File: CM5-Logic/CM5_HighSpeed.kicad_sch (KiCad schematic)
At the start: 12 parts, among them J11 690-019-298-412, J12 USB3_A, U3 AP22653W6, U4 RT9742SNGV

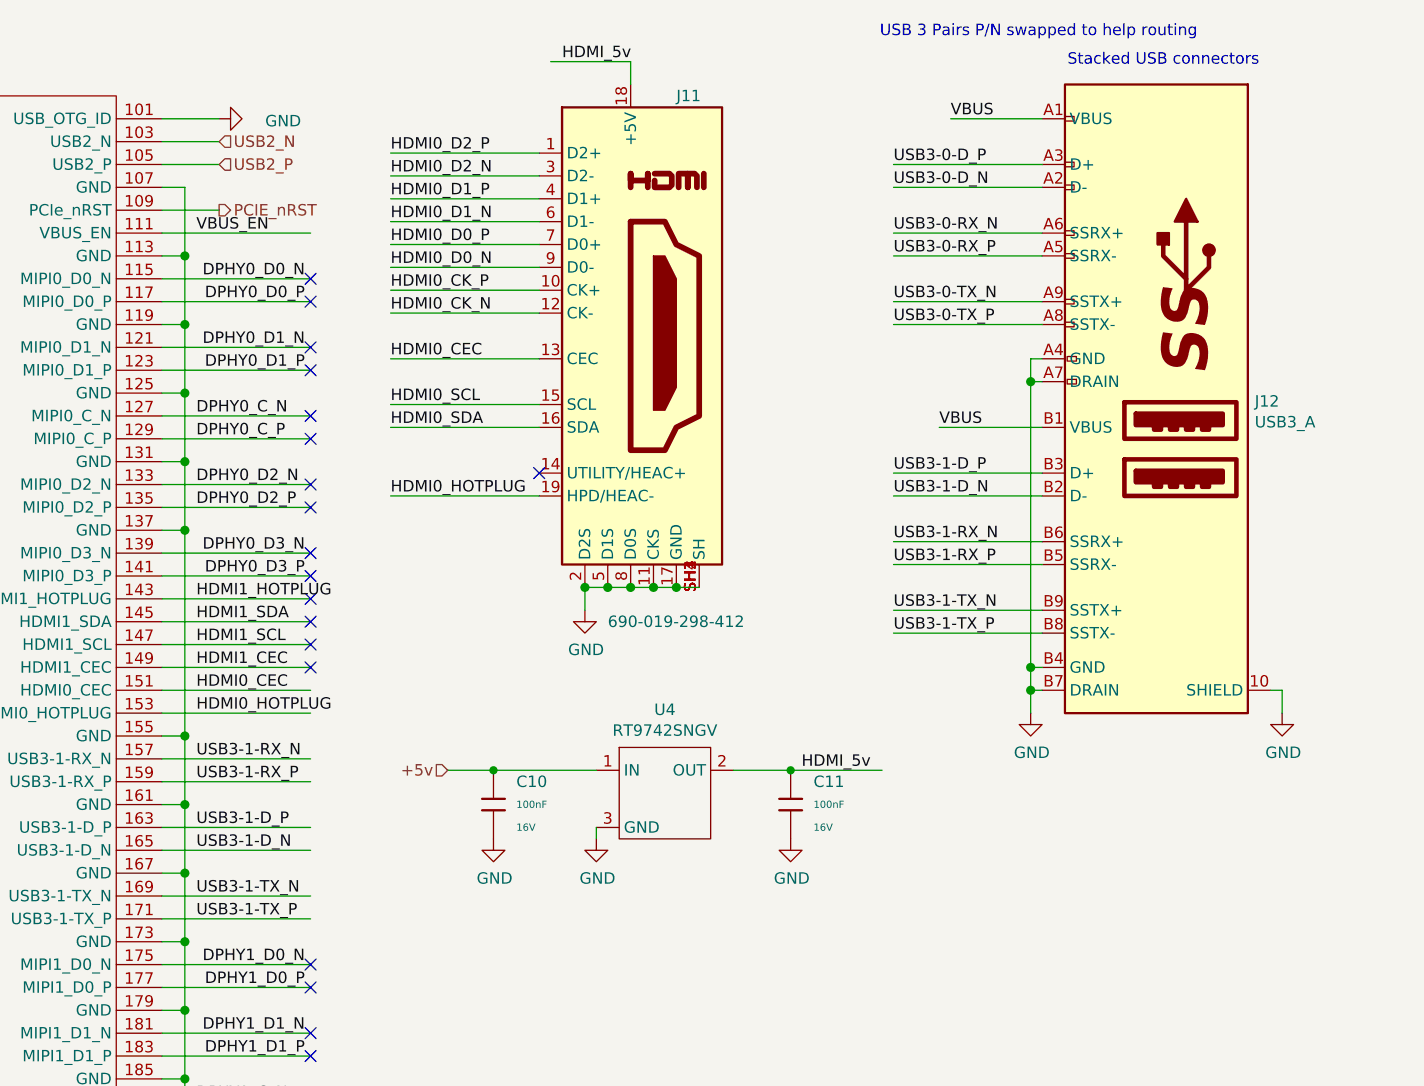
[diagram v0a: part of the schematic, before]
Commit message: adds respeaker and reworks the amplifier
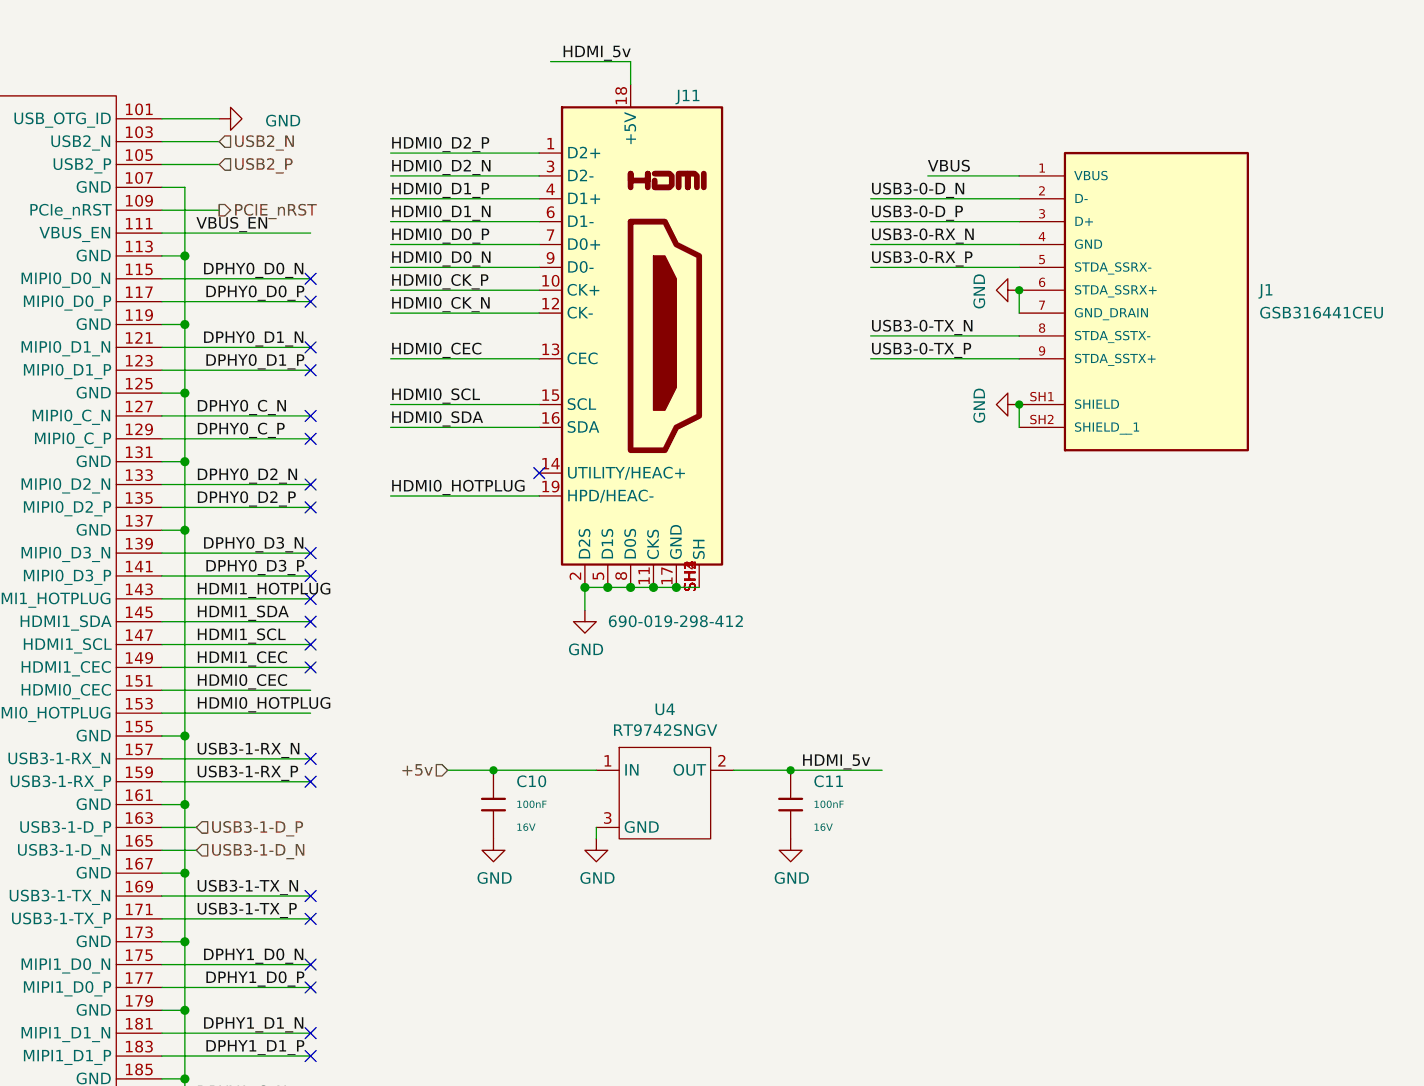
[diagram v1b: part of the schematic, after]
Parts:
- removed J12: USB3_A, CM5IO:MTCONN_UBAF30-D2011, symbol CM5IO:USB3_A
- added J1: GSB316441CEU, Custom Components:AMPHENOL_GSB316441CEU, symbol GSB316441CEU:GSB316441CEU
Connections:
- net GND: now also J1.6 (STDA_SSRX+), J1.7 (GND_DRAIN), J1.SH1 (SHIELD), J1.SH2 (SHIELD__1)
- net USB3-0-D_N: now also J1.2 (D-)
- net USB3-0-D_P: now also J1.3 (D+)
- net USB3-0-RX_N: now also J1.4 (GND)
- net USB3-0-RX_P: now also J1.5 (STDA_SSRX-)
- net USB3-0-TX_N: now also J1.8 (STDA_SSTX-)
- net USB3-0-TX_P: now also J1.9 (STDA_SSTX+)
- net VBUS: now also J1.1 (VBUS)
- no-connect marks 34 -> 38
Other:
- note removed: "Stacked USB connectors"
- note removed: "USB 3 Pairs P/N swapped to help routing"

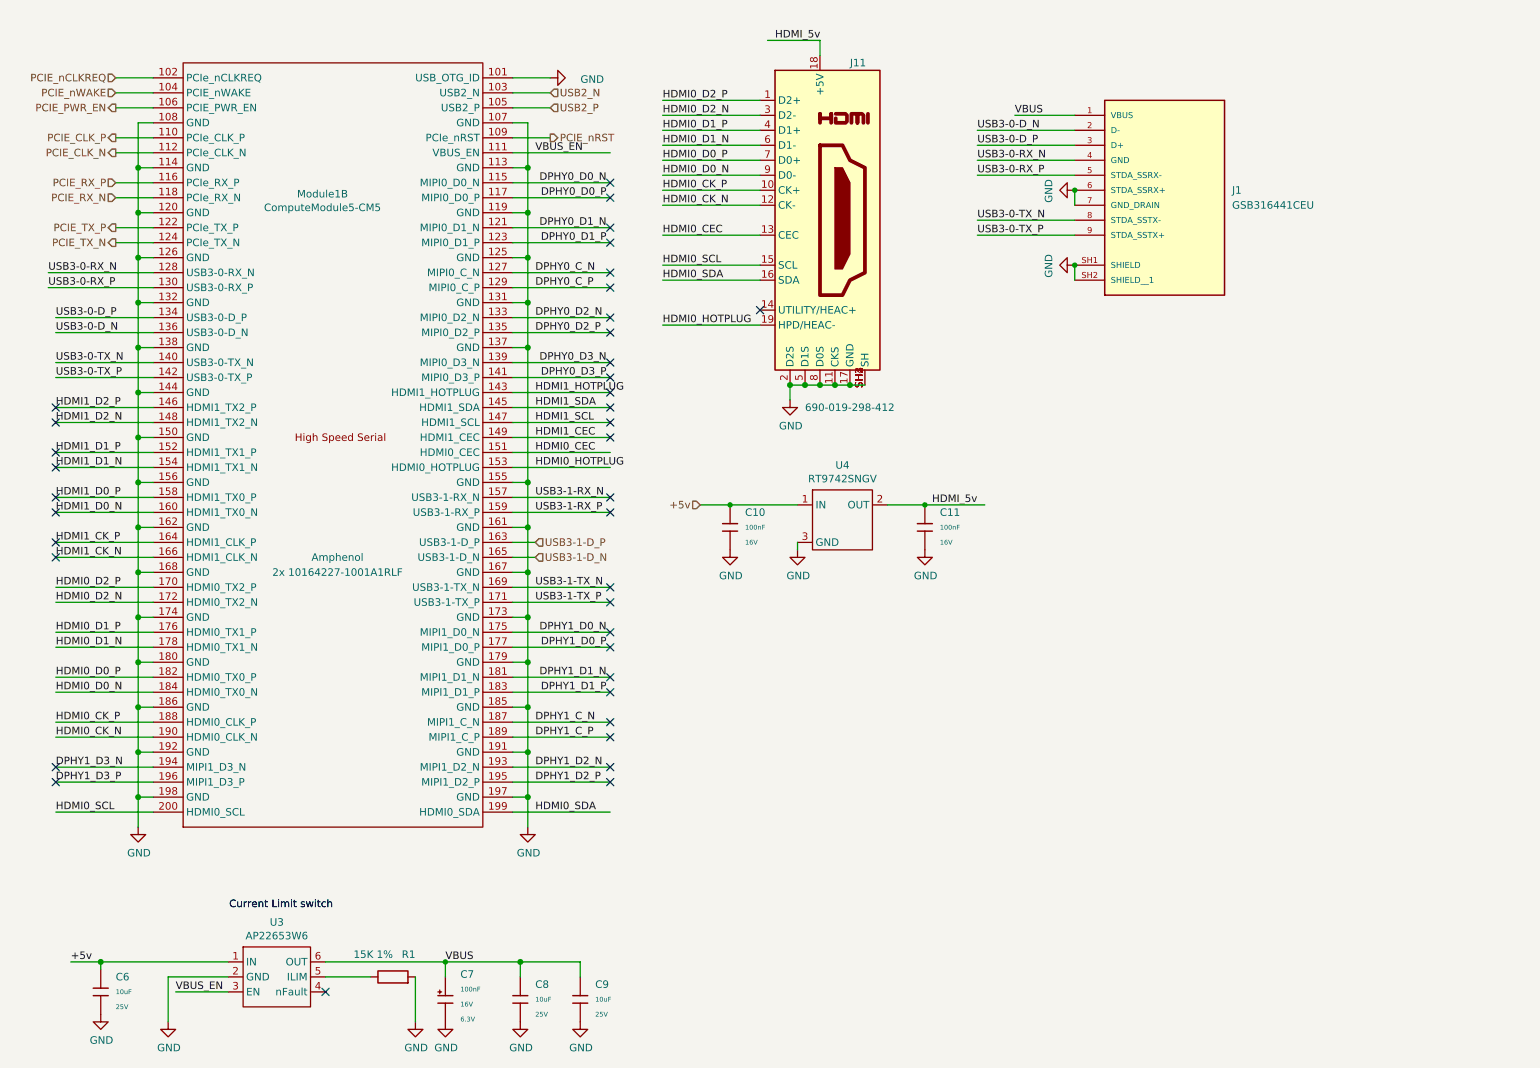
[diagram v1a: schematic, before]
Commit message: fixes all label issues and power input pins
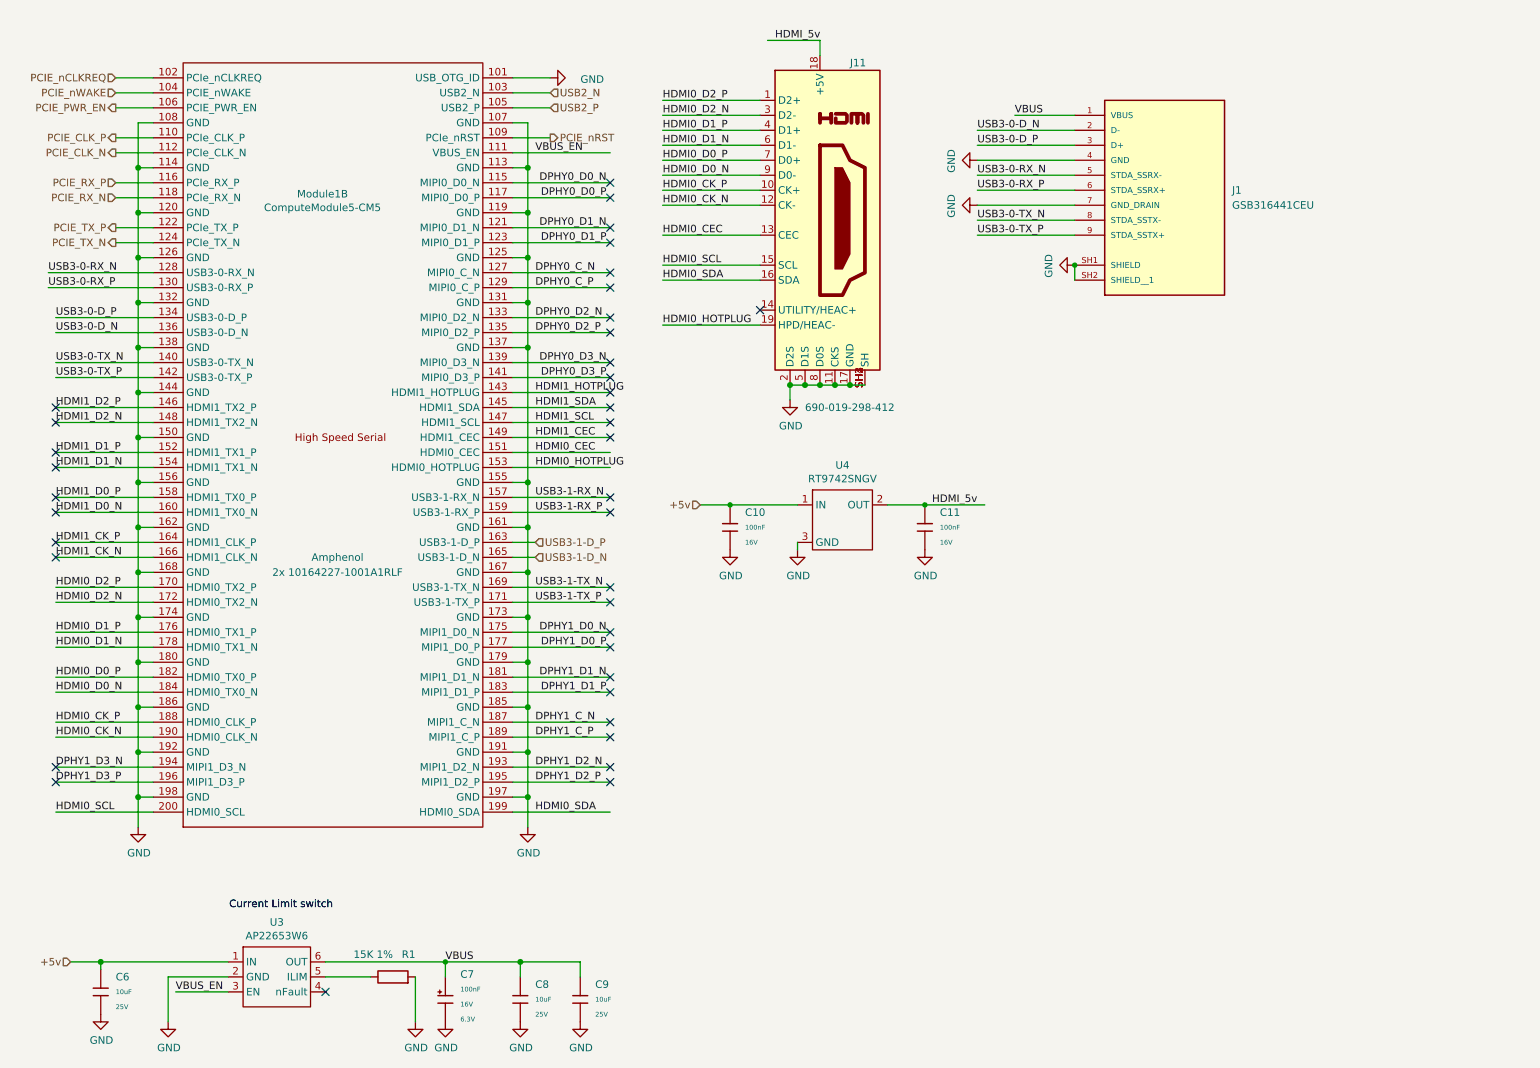
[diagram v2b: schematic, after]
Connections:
- net GND: now also J1.4 (GND); no longer J1.6 (STDA_SSRX+)
- net USB3-0-RX_N: now also J1.5 (STDA_SSRX-); no longer J1.4 (GND)
- net USB3-0-RX_P: now also J1.6 (STDA_SSRX+); no longer J1.5 (STDA_SSRX-)
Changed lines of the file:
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@@
 	)
 	(junction
-		(at 194.31 44.45)
-		(diameter 0)
-		(color 0 0 0 0)
-	)
-	(junction
 		(at 35.56 40.64)
 		(diameter 1.016)
@@
 	(wire
 		(pts
-			(xy 177.8 39.37) (xy 194.31 39.37)
-		)
-		(stroke
-			(width 0)
-			(type solid)
-		)
-	)
-	(wire
-		(pts
 			(xy 21.59 83.82) (xy 38.1 83.82)
 		)
@@
 	(wire
 		(pts
+			(xy 177.8 46.99) (xy 194.31 46.99)
+		)
+		(stroke
+			(width 0)
+			(type default)
+		)
+	)
+	(wire
+		(pts
 			(xy 99.06 68.58) (xy 115.57 68.58)
 		)
@@
 	(wire
 		(pts
-			(xy 177.8 41.91) (xy 194.31 41.91)
+			(xy 21.59 144.78) (xy 38.1 144.78)
 		)
 		(stroke
@@
 	(wire
 		(pts
-			(xy 21.59 144.78) (xy 38.1 144.78)
+			(xy 177.8 41.91) (xy 194.31 41.91)
 		)
 		(stroke
@@
 	(wire
 		(pts
+			(xy 177.8 39.37) (xy 194.31 39.37)
+		)
+		(stroke
+			(width 0)
+			(type default)
+		)
+	)
+	(wire
+		(pts
 			(xy 124.46 57.15) (xy 140.97 57.15)
 		)
@@
 	(wire
 		(pts
-			(xy 194.31 44.45) (xy 194.31 46.99)
-		)
-		(stroke
-			(width 0)
-			(type default)
-		)
-	)
-	(wire
-		(pts
 			(xy 177.8 36.83) (xy 194.31 36.83)
 		)
@@
 	(wire
 		(pts
+			(xy 177.8 44.45) (xy 194.31 44.45)
+		)
+		(stroke
+			(width 0)
+			(type solid)
+		)
+	)
+	(wire
+		(pts
 			(xy 99.06 147.32) (xy 101.6 147.32)
 		)
@@
 		)
 	)
-	(label "HDMI0_D2_P"
-		(at 21.59 111.76 0)
+	(label "USB3-0-RX_P"
+		(at 177.8 44.45 0)
 		(effects
 			(font
@@
 		)
 	)
-	(label "DPHY1_D2_N"
-		(at 102.87 142.24 0)
+	(label "HDMI0_D2_P"
+		(at 21.59 111.76 0)
 		(effects
 			(font
@@
 		)
 	)
-	(label "USB3-0-RX_P"
-		(at 177.8 41.91 0)
+	(label "DPHY1_D2_N"
+		(at 102.87 142.24 0)
 		(effects
 			(font
@@
 		)
 	)
-	(label "+5v"
-		(at 24.13 175.26 0)
-		(effects
-			(font
-				(size 1.27 1.27)
-			)
-			(justify left bottom)
-		)
-	)
 	(label "HDMI0_CK_P"
 		(at 21.59 134.62 0)
@@
 		)
 	)
-	(label "USB3-0-RX_N"
-		(at 177.8 39.37 0)
-		(effects
-			(font
-				(size 1.27 1.27)
-			)
-			(justify left bottom)
-		)
-	)
 	(label "HDMI1_D2_N"
 		(at 21.59 83.82 0)
@@
 		)
 	)
+	(label "USB3-0-RX_N"
+		(at 177.8 41.91 0)
+		(effects
+			(font
+				(size 1.27 1.27)
+			)
+			(justify left bottom)
+		)
+	)
 	(label "VBUS"
 		(at 184.15 31.75 0)
@@
 		)
 	)
+	(hierarchical_label "+5v"
+		(shape input)
+		(at 24.13 175.26 180)
+		(effects
+			(font
+				(size 1.27 1.27)
+			)
+			(justify right)
+		)
+	)
 	(hierarchical_label "PCIE_nWAKE"
 		(shape input)
@@
 	)
 	(symbol
+		(lib_id "power:GND")
+		(at 177.8 39.37 270)
+		(unit 1)
+		(exclude_from_sim no)
+		(in_bom yes)
+		(on_board yes)
+		(dnp no)
+		(property "Reference" "#PWR068"
+			(at 171.45 39.37 0)
+			(effects
+				(font
+					(size 1.27 1.27)
+				)
+				(hide yes)
+			)
+		)
+		(property "Value" "GND"
+			(at 173.4058 39.497 0)
+			(effects
+				(font
+					(size 1.27 1.27)
+				)
+			)
+		)
+		(property "Footprint" ""
+			(at 177.8 39.37 0)
+			(effects
+				(font
+					(size 1.27 1.27)
+				)
+				(hide yes)
+			)
+		)
+		(property "Datasheet" ""
+			(at 177.8 39.37 0)
+			(effects
+				(font
+					(size 1.27 1.27)
+				)
+				(hide yes)
+			)
+		)
+		(property "Description" "Power symbol creates a global label with name \"GND\" , ground"
+			(at 177.8 39.37 0)
+			(effects
+				(font
+					(size 1.27 1.27)
+				)
+				(hide yes)
+			)
+		)
+		(pin "1"
+		)
+		(instances
+			(project "CM5IO"
+				(path "/e63e39d7-6ac0-4ffd-8aa3-1841a4541b55/00000000-0000-0000-0000-00005cff70b1"
+					(reference "#PWR068")
+					(unit 1)
+				)
+			)
+		)
+	)
+	(symbol
 		(lib_id "PCM_JLCPCB-Capacitors:0805,10uF")
 		(at 110.49 181.61 0)
@@
 	(symbol
 		(lib_id "power:GND")
-		(at 194.31 44.45 270)
+		(at 177.8 46.99 270)
 		(unit 1)
 		(exclude_from_sim no)
@@
 		(dnp no)
 		(property "Reference" "#PWR05"
-			(at 187.96 44.45 0)
+			(at 171.45 46.99 0)
 			(effects
 				(font
@@
 		)
 		(property "Value" "GND"
-			(at 189.9158 44.577 0)
+			(at 173.4058 47.117 0)
 			(effects
 				(font
@@
 		)
 		(property "Footprint" ""
-			(at 194.31 44.45 0)
+			(at 177.8 46.99 0)
 			(effects
 				(font
@@
 		)
 		(property "Datasheet" ""
-			(at 194.31 44.45 0)
+			(at 177.8 46.99 0)
 			(effects
 				(font
@@
 		)
 		(property "Description" "Power symbol creates a global label with name \"GND\" , ground"
-			(at 194.31 44.45 0)
+			(at 177.8 46.99 0)
 			(effects
 				(font

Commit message: changes USB port, adds TMC2209 SilentStepStick footprint, redoes PCB Layout
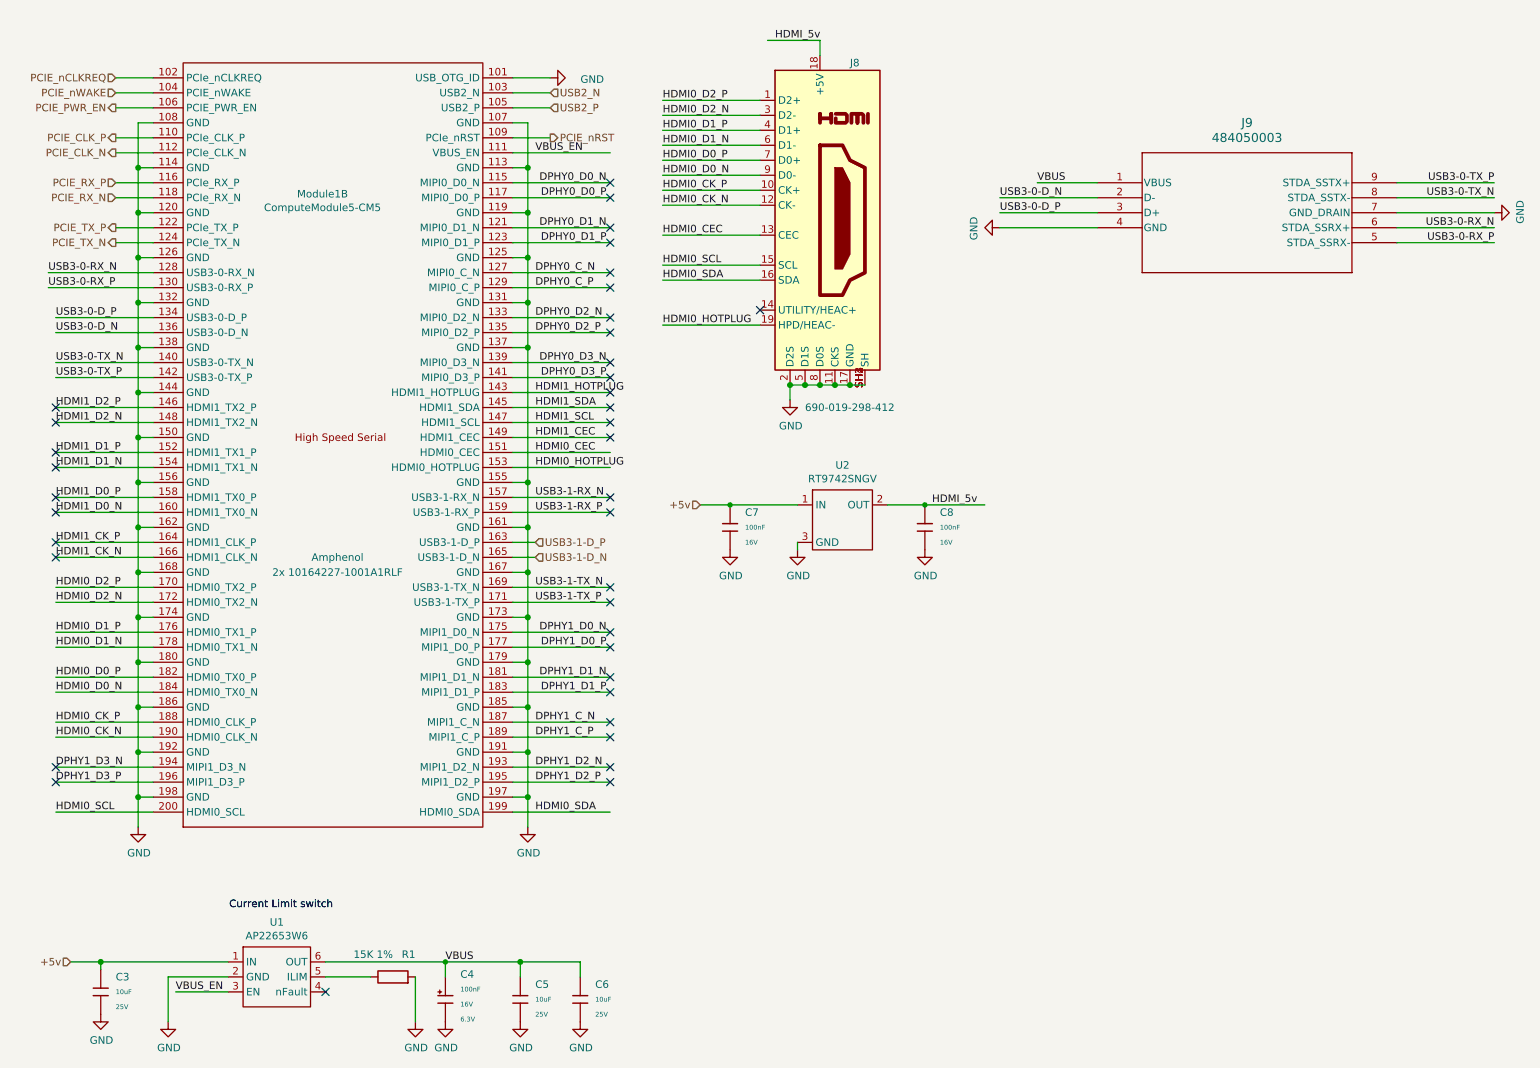
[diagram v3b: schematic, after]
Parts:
- removed J1: GSB316441CEU, Custom Components:AMPHENOL_GSB316441CEU, symbol GSB316441CEU:GSB316441CEU
- added J9: 484050003, Custom Components:484050003_MOL, symbol 484050003_MOL:484050003
- renumbered C6 to C3, C7 to C4, C8 to C5, C9 to C6, C10 to C7, C11 to C8, J11 to J8, U3 to U1, U4 to U2
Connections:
- net GND: now also J9.4 (GND), J9.7 (GND_DRAIN)
- net USB3-0-D_N: now also J9.2 (D-)
- net USB3-0-D_P: now also J9.3 (D+)
- net USB3-0-RX_N: now also J9.6 (STDA_SSRX+)
- net USB3-0-RX_P: now also J9.5 (STDA_SSRX-)
- net USB3-0-TX_N: now also J9.8 (STDA_SSTX-)
- net USB3-0-TX_P: now also J9.9 (STDA_SSTX+)
- net VBUS: now also J9.1 (VBUS)
